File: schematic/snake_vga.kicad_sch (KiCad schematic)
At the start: 8 parts, among them Q1 TN2106, Q2 TN2106, U1 NUCLEO-LxxxKx, U2 UPduino_v3.1, U3 SLP120B16-16

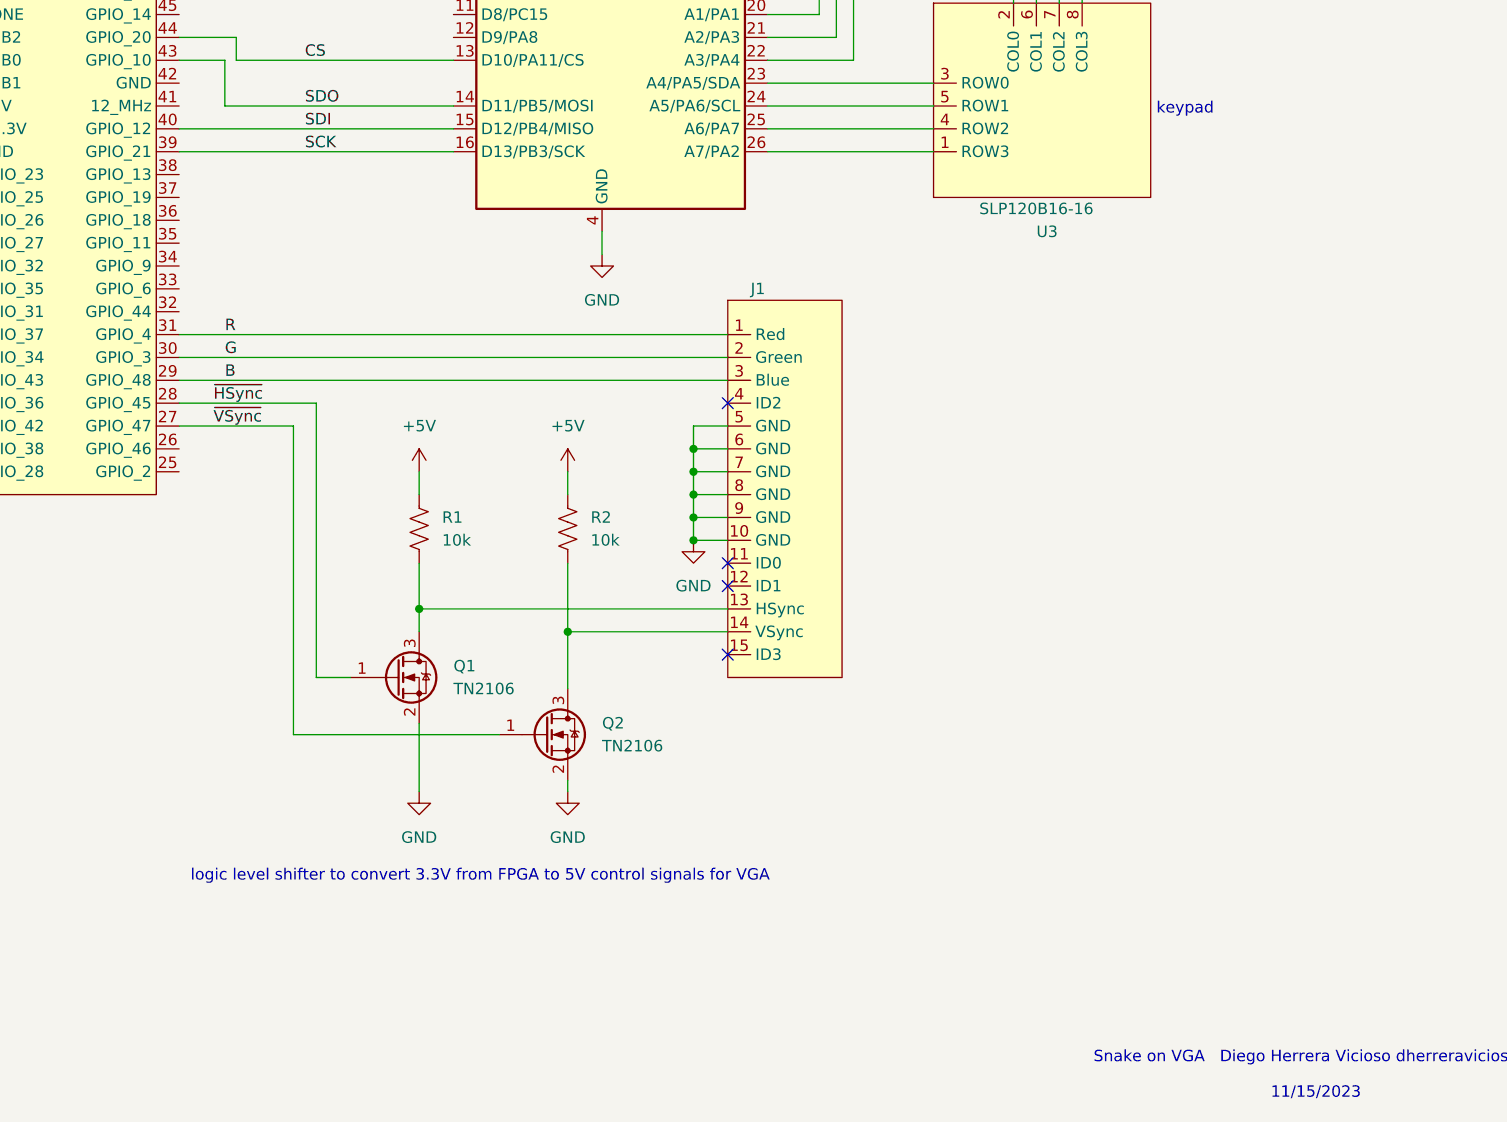
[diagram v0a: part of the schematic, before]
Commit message: updated RGB resistor network
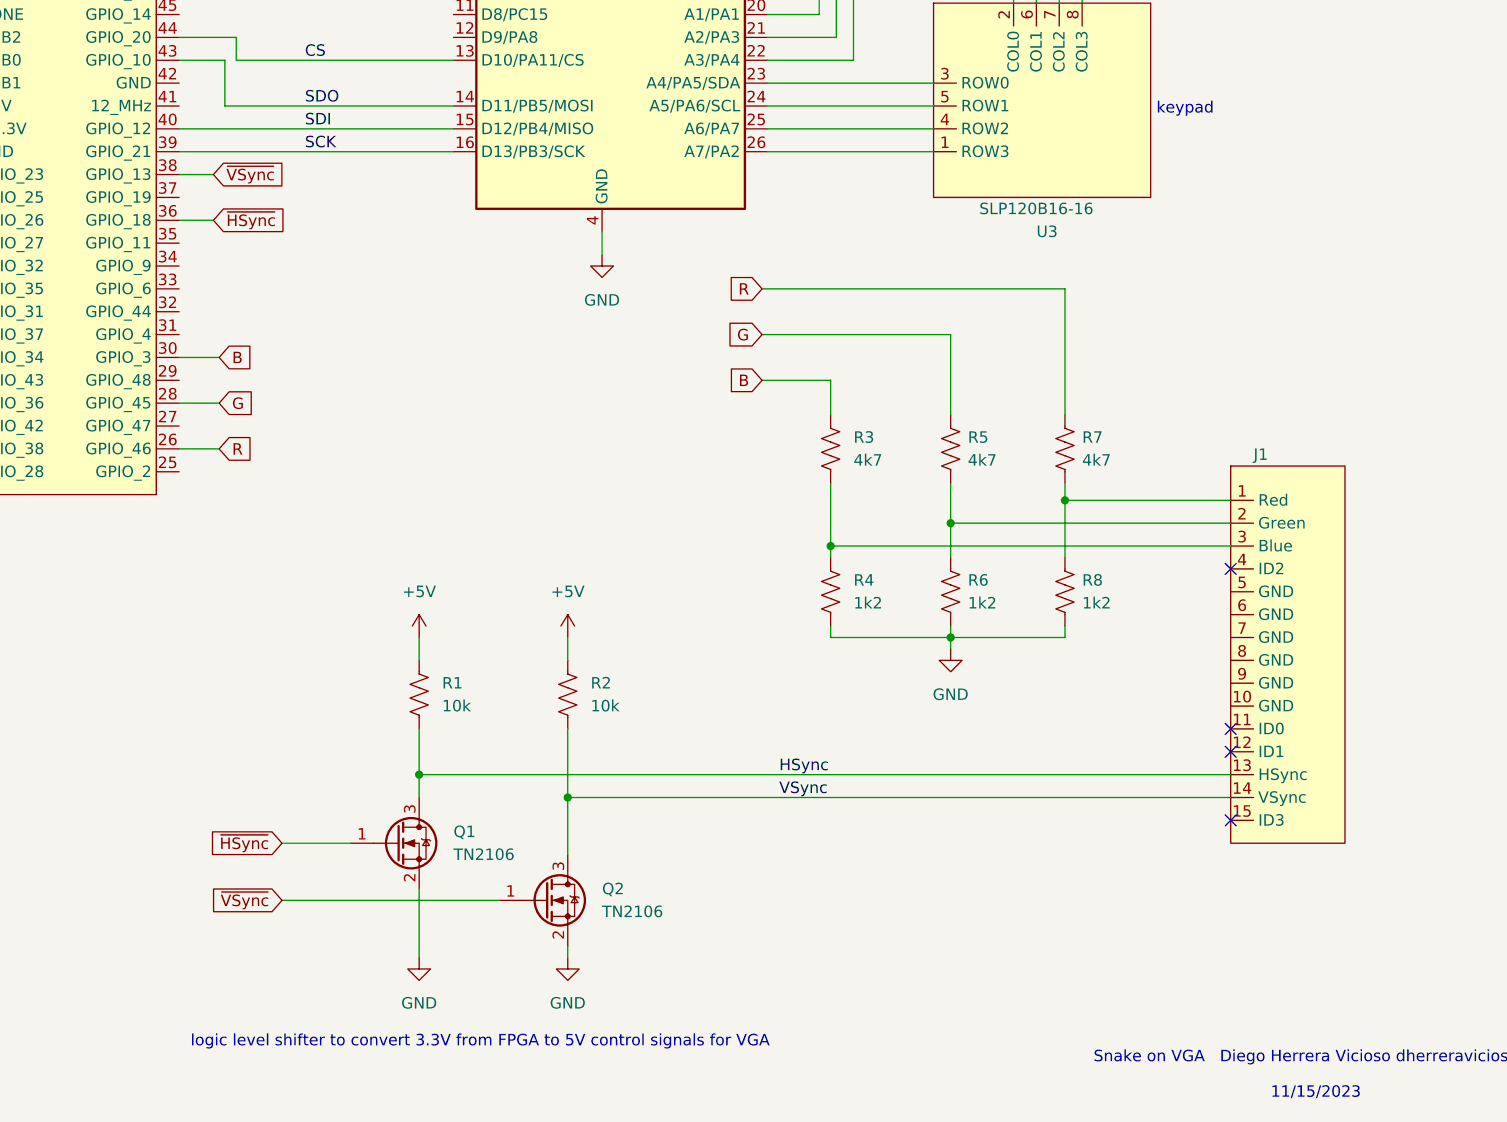
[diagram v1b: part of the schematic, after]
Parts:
- added R3, R5, R7: 4k7, symbol Device:R_US
- added R4, R6, R8: 1k2, symbol Device:R_US
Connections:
- net B: now also U2.30 (GPIO_3), R3.1; no longer J1.3 (Blue), U2.29 (GPIO_48)
- net G: now also U2.28 (GPIO_45), R5.1; no longer J1.2 (Green), U2.30 (GPIO_3)
- net GND: now also R4.2, R6.2, R8.2; no longer J1.10 (GND), J1.5 (GND), J1.6 (GND), J1.7 (GND), J1.8 (GND), J1.9 (GND)
- net R: now also U2.26 (GPIO_46), R7.1; no longer J1.1 (Red), U2.31 (GPIO_4)
- net ~{HSync}: now also U2.36 (GPIO_18); no longer U2.28 (GPIO_45)
- net ~{VSync}: now also U2.38 (GPIO_13); no longer U2.27 (GPIO_47)
- net HSync: now reaches J1.13 (HSync), Q1.3 (D), R1.2
- net VSync: now reaches J1.14 (VSync), Q2.3 (D), R2.2
- new net: J1.3 (Blue), R3.2, R4.1
- new net: J1.1 (Red), R7.2, R8.1
- new net: J1.2 (Green), R5.2, R6.1
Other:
- moved on the sheet: J1, Q1, Q2, R1, R2

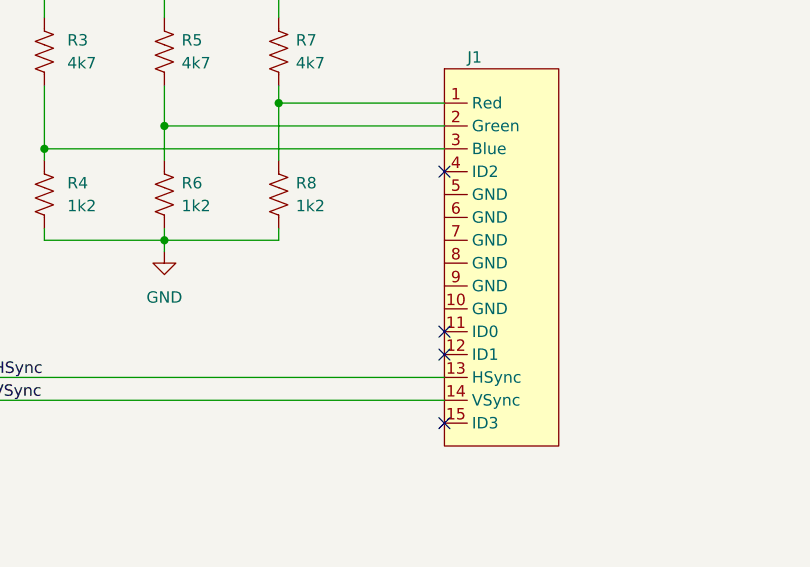
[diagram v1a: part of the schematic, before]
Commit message: updated grounds on VGA connector
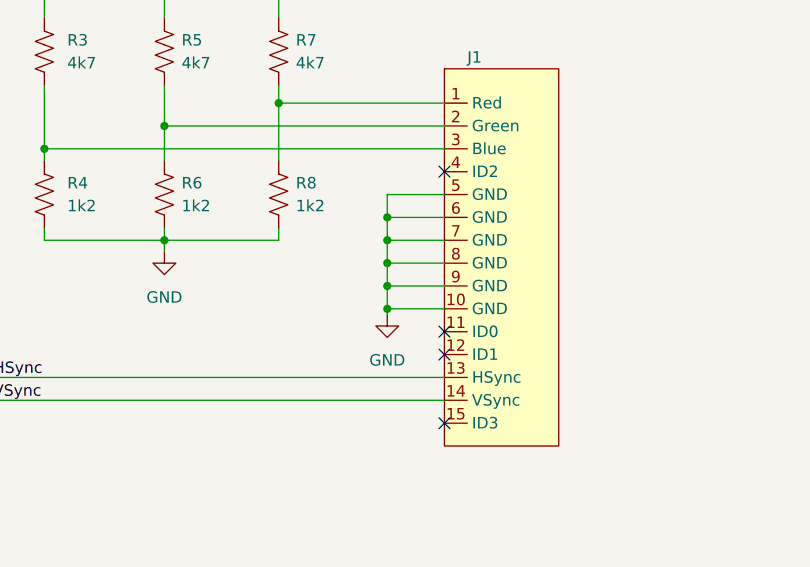
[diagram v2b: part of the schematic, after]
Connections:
- net GND: now also J1.10 (GND), J1.5 (GND), J1.6 (GND), J1.7 (GND), J1.8 (GND), J1.9 (GND)
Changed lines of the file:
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@@
 (kicad_sch (version 20230121) (generator eeschema)
   (paper "A4")
+  (junction (at 195.58 147.955) (diameter 0) (color 0 0 0 0)
+  )
+  (junction (at 195.58 140.335) (diameter 0) (color 0 0 0 0)
+  )
   (junction (at 183.515 127.635) (diameter 0) (color 0 0 0 0)
   )
+  (junction (at 195.58 150.495) (diameter 0) (color 0 0 0 0)
+  )
+  (junction (at 195.58 142.875) (diameter 0) (color 0 0 0 0)
+  )
   (junction (at 128.27 160.655) (diameter 0) (color 0 0 0 0)
   )
   (junction (at 170.815 142.875) (diameter 0) (color 0 0 0 0)
+  )
+  (junction (at 195.58 145.415) (diameter 0) (color 0 0 0 0)
   )
   (junction (at 111.76 158.115) (diameter 0) (color 0 0 0 0)
@@
     (stroke (width 0) (type default))
   )
+  (wire (pts (xy 195.58 145.415) (xy 195.58 147.955))
+    (stroke (width 0) (type default))
+  )
   (wire (pts (xy 52.07 88.9) (xy 52.07 90.17))
     (stroke (width 0) (type default))
@@
     (stroke (width 0) (type default))
   )
+  (wire (pts (xy 201.93 150.495) (xy 195.58 150.495))
+    (stroke (width 0) (type default))
+  )
   (wire (pts (xy 150.495 81.28) (xy 168.91 81.28))
     (stroke (width 0) (type default))
   )
+  (wire (pts (xy 195.58 147.955) (xy 195.58 150.495))
+    (stroke (width 0) (type default))
+  )
   (wire (pts (xy 150.495 76.2) (xy 158.115 76.2))
     (stroke (width 0) (type default))
@@
     (stroke (width 0) (type default))
   )
+  (wire (pts (xy 195.58 142.875) (xy 195.58 145.415))
+    (stroke (width 0) (type default))
+  )
   (wire (pts (xy 128.27 177.165) (xy 128.27 178.435))
     (stroke (width 0) (type default))
@@
     (stroke (width 0) (type default))
   )
+  (wire (pts (xy 195.58 147.955) (xy 201.93 147.955))
+    (stroke (width 0) (type default))
+  )
   (wire (pts (xy 85.09 116.84) (xy 89.535 116.84))
     (stroke (width 0) (type default))
@@
     (stroke (width 0) (type default))
   )
+  (wire (pts (xy 195.58 140.335) (xy 201.93 140.335))
+    (stroke (width 0) (type default))
+  )
   (wire (pts (xy 59.69 88.9) (xy 52.07 88.9))
     (stroke (width 0) (type default))
   )
+  (wire (pts (xy 195.58 145.415) (xy 201.93 145.415))
+    (stroke (width 0) (type default))
+  )
   (wire (pts (xy 154.305 71.12) (xy 150.495 71.12))
     (stroke (width 0) (type default))
@@
     (stroke (width 0) (type default))
   )
+  (wire (pts (xy 201.93 137.795) (xy 195.58 137.795))
+    (stroke (width 0) (type default))
+  )
   (wire (pts (xy 185.42 72.39) (xy 185.42 65.405))
     (stroke (width 0) (type default))
@@
     (stroke (width 0) (type default))
   )
+  (wire (pts (xy 195.58 137.795) (xy 195.58 140.335))
+    (stroke (width 0) (type default))
+  )
   (wire (pts (xy 150.495 86.36) (xy 168.91 86.36))
     (stroke (width 0) (type default))
@@
     (stroke (width 0) (type default))
   )
+  (wire (pts (xy 195.58 140.335) (xy 195.58 142.875))
+    (stroke (width 0) (type default))
+  )
+  (wire (pts (xy 195.58 142.875) (xy 201.93 142.875))
+    (stroke (width 0) (type default))
+  )
   (wire (pts (xy 154.305 65.405) (xy 154.305 71.12))
     (stroke (width 0) (type default))
@@
   )
   (wire (pts (xy 150.495 88.9) (xy 168.91 88.9))
+    (stroke (width 0) (type default))
+  )
+  (wire (pts (xy 195.58 150.495) (xy 195.58 151.13))
     (stroke (width 0) (type default))
   )
@@
         )
       )
+    )
+  )
+  (symbol (lib_id "power:GND") (at 195.58 151.13 0) (unit 1)
+    (in_bom yes) (on_board yes) (dnp no) (fields_autoplaced)
+    (property "Reference" "#PWR010" (at 195.58 157.48 0)
+      (effects (font (size 1.27 1.27)) hide)
+    )
+    (property "Value" "GND" (at 195.58 156.21 0)
+      (effects (font (size 1.27 1.27)))
+    )
+    (property "Footprint" "" (at 195.58 151.13 0)
+      (effects (font (size 1.27 1.27)) hide)
+    )
+    (property "Datasheet" "" (at 195.58 151.13 0)
+      (effects (font (size 1.27 1.27)) hide)
+    )
+    (pin "1")
+    (instances
+      (project "snake_vga"
+        (path "/050d2bec-4ed1-4650-8720-e98c77b61d9d"
+          (reference "#PWR010") (unit 1)
+        )
+      )

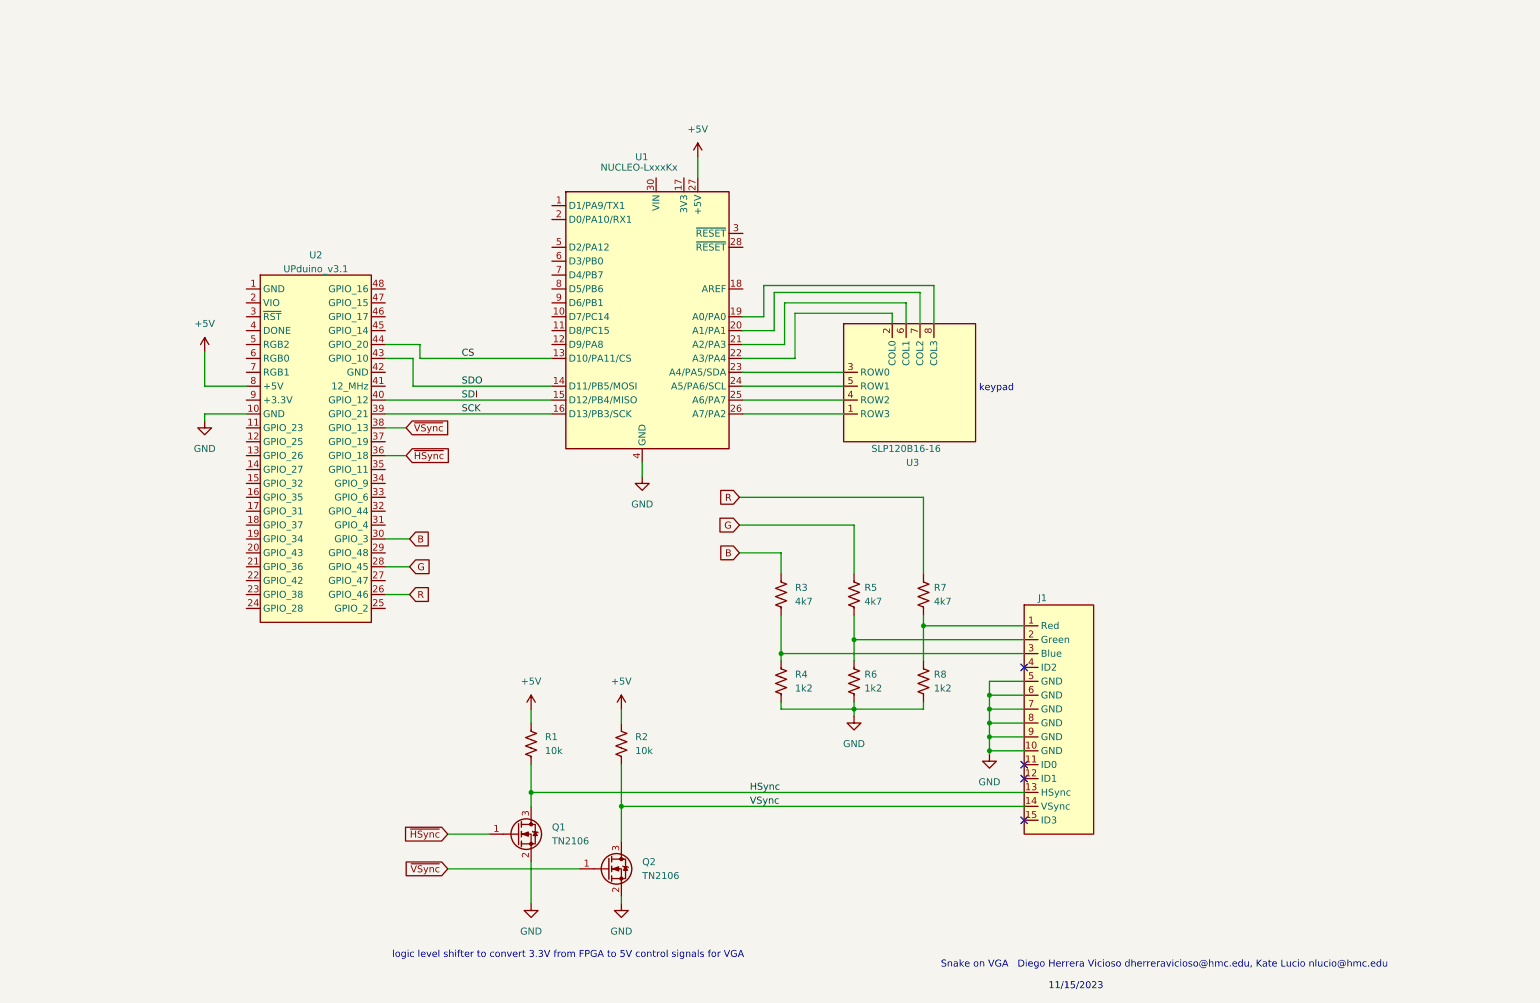
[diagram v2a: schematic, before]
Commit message: Moved to center of screen
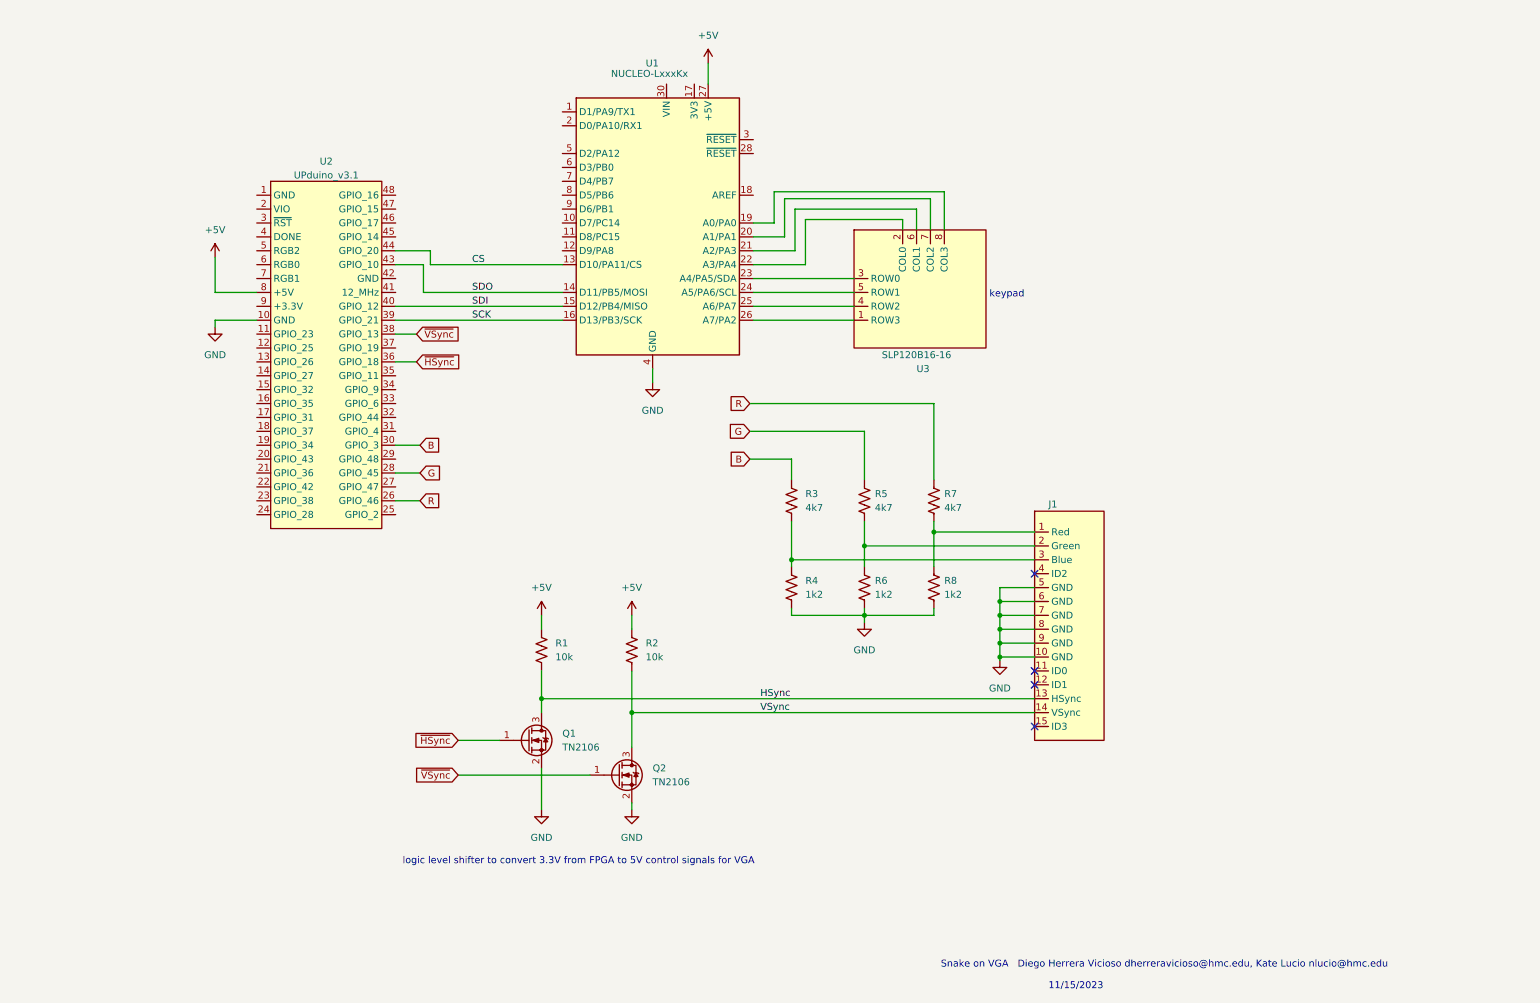
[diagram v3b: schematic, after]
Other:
- moved on the sheet: J1, Q1, Q2, R1, R2, R3, R4, R5, R6, R7, R8, U1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
